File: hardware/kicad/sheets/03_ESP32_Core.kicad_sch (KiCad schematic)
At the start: 0 parts

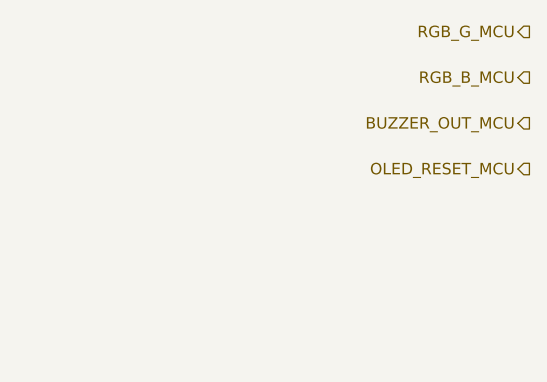
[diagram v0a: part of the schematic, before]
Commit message: Resolve Rev A power control interfaces
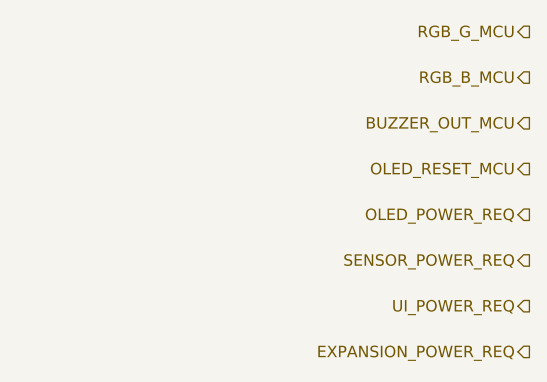
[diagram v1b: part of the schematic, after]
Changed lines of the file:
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@@
+    (effects (font (size 1.27 1.27)) (justify right))
+  )
+  (hierarchical_label "OLED_POWER_REQ" (shape output) (at 180 126.28 180)
+    (effects (font (size 1.27 1.27)) (justify right))
+  )
+  (hierarchical_label "SENSOR_POWER_REQ" (shape output) (at 180 131.36 180)
+    (effects (font (size 1.27 1.27)) (justify right))
+  )
+  (hierarchical_label "UI_POWER_REQ" (shape output) (at 180 136.44 180)
+    (effects (font (size 1.27 1.27)) (justify right))
+  )
+  (hierarchical_label "EXPANSION_POWER_REQ" (shape output) (at 180 141.52 180)
     (effects (font (size 1.27 1.27)) (justify right))
   )

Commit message: Implement ESP32-S3 core subsystem
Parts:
- added C1: 22 µF effective bulk, symbol IPC100:C
- added C2: 1 µF X7R, symbol IPC100:C
- added C3: 100 nF X7R, symbol IPC100:C
- added C4: 1 µF EN RC starting value, symbol IPC100:C
- added C5: 10 nF CT — 100 ms target, verify suffix/equation, symbol IPC100:C
- added C6: 100 nF supervisor bypass, symbol IPC100:C
- added R1: 10 kΩ EN/reset pull-up, symbol IPC100:R
- added R2: 10 kΩ GPIO0 boot pull-up, symbol IPC100:R
- added R3: 22 Ω USB D- tuning, symbol IPC100:R
- added R4: 22 Ω USB D+ tuning, symbol IPC100:R
- added R5: 499 Ω UART0 TX EMC series, symbol IPC100:R
- added SW1: RESET — momentary NO, symbol IPC100:SW
- added SW2: BOOT — momentary NO, symbol IPC100:SW
- added U1: ESP32-S3-WROOM-1-N8, symbol IPC100:ESP32S3WROOM1
- added U2: TPS389030-Q1 2.89 V typ / 100 ms target, symbol IPC100:TPS3890
- added U3: TPD2EUSB30 low-capacitance ESD boundary, symbol IPC100:TPD2EUSB30
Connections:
- net +3V3_CORE: now also C1.2, C2.2, C3.2, C6.2, R1.2, R2.2, U1.19 (GPIO11), U2.1 (VDD), U2.2 (SENSE), U2.3 (MR)
- net ARM_IN_COND: now also U1.9 (GPIO16)
- net AXIS1_LEN_MCU: now also U1.10 (GPIO17)
- net AXIS1_LPWM_MCU: now also U1.40 (GND)
- net AXIS1_REN_MCU: now also U1.11 (GPIO18)
- net AXIS1_RPWM_MCU: now also U1.41 (EPAD_GND)
- net AXIS2_LEN_MCU: now also U1.31 (GPIO38)
- net AXIS2_LPWM_MCU: now also U1.12 (GPIO8)
- net AXIS2_REN_MCU: now also U1.39 (GPIO1_ADC1_CH0)
- net AXIS2_RPWM_MCU: now also U1.13 (GPIO19_USB_D-)
- net BATTERY_SENSE: now also U1.23 (GPIO21)
- net ENCODER_A_COND: now also U1.3 (EN_CHIP_PU)
- net ENCODER_B_COND: now also U1.2 (3V3)
- net ENCODER_SW_COND: now also U1.1 (GND)
- net ESP_BOOT: now also R2.1, SW2.2, U1.35 (GPIO42_RESERVED)
- net ESP_EN: now also C4.2, R1.1, SW1.2, U1.18 (GPIO10), U2.6 (GND)
- net EXPANSION_POWER_REQ: now also U1.28 (GPIO35)
- net FIRE_IN_COND: now also U1.4 (GPIO4)
- net I2C_SCL: now also U1.37 (GPIO43_U0TXD)
- net I2C_SDA: now also U1.38 (GPIO2)
- net LIMIT_DOWN_COND: now also U1.14 (GPIO20_USB_D+)
- net LIMIT_LEFT_COND: now also U1.17 (GPIO9)
- net LIMIT_RIGHT_COND: now also U1.16 (GPIO46_STRAP)
- net LIMIT_UP_COND: now also U1.15 (GPIO3_STRAP)
- net OLED_POWER_REQ: now also U1.34 (GPIO41)
- net RELAY_CMD_MCU: now also U1.30 (GPIO37_RESERVED)
- net SENSOR_POWER_REQ: now also U1.33 (GPIO40)
- net STOP_IN_COND: now also U1.24 (GPIO47)
- net UART0_RX: now also U1.26 (GPIO45_STRAP)
- net UART0_TX: now also R5.1
- net UI_POWER_REQ: now also U1.29 (GPIO36)
- net USB_D+: now also R4.2, U3.1 (D-)
- net USB_D-: now also R3.2, U3.2 (D+)
- new net CORE_RESET_CT: C5.2, U2.5 (CT)
- new net GND: C1.1, C2.1, C3.1, C4.1, C5.1, C6.1, SW1.1, SW2.1, U1.20 (GPIO12), U1.21 (GPIO13), U1.22 (GPIO14), U2.4 (RESET_N), U3.3 (GND)
- new net UART0_TX_MCU: R5.2, U1.25 (GPIO48)
- new net USB_D+_MCU: R4.1, U1.7 (GPIO7)
- new net USB_D-_MCU: R3.1, U1.8 (GPIO15)
- no-connect marks 0 -> 5
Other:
- note added: "1 — ESP32-S3-WROOM-1-N8 CORE (8 MB QSPI FLASH, NO PSRAM, NO EXTERNAL CRYSTAL)"
- note added: "2 — CORE SUPPLY DECOUPLING (PLACE AT MODULE 3V3/GND PINS)"
- note added: "3 — CORE SUPERVISOR, EN/RESET, BOOT STRAP"
- note added: "4 — MCU-SIDE USB 2.0 SERIAL/JTAG AND UART0 RECOVERY"
- note added: "5 — HIERARCHICAL FUNCTIONAL INTERFACES (RAW GPIO IDENTIFIERS TERMINATE ABOVE)"
- note added: "Functional net names only cross the sheet boundary. MAIN_POWER_GOOD, MAIN_INPUT_VALID, POWER_FAULT_SUMMARY, RGB, buzzer, OLED reset, future communications, and physical connectors are intentionally absent."
- note added: "GPIO3 / GPIO45 / GPIO46 remain unconnected straps. GPIO37 / GPIO42 remain unconnected future reserve. EPAD and both module GND pins bond directly to the logic ground plane."
- note added: "Keep module antenna keepout free of copper, components, enclosure metal, and harnesses per Espressif guidance. Footprint and PCB keepout intentionally deferred."
- note added: "Native USB Serial/JTAG is the approved JTAG/debug path. No traditional JTAG pins or debugger connector are added. Sheet 09 owns USB-C, CC, shield, external pinout, and fixture contacts."
- note added: "No separate analog rail exists on ESP32-S3-WROOM-1-N8. The module integrates crystal, flash, and internal supply support; add no external oscillator or invented analog regulator."
- note added: "Normal boot: GPIO0 released high. Joint download recovery: hold BOOT/GPIO0 low, pulse RESET/EN low, release EN, then release BOOT. GPIO3/45/46 remain unloaded."
- note added: "RESET_VALID is the active-high, pulled-up supervisor release/EN node. It proves hardware reset release and readiness to begin instruction execution; it does not prove application initialization."
- note added: "UART0 RX is direct 3.3 V fixture input; the fixture shall never drive an unpowered module. UART0 TX may emit ROM boot messages. R5 follows Espressif's preliminary EMC guidance."
- note removed: "Detailed implementation intentionally deferred to subsequent engineering package."
- note removed: "PACKAGE 01 PLACEHOLDER — NO CIRCUITRY OR FOOTPRINTS"
- title: IPC-100 Rev A — 03 ESP32 Core -> IPC-100 Rev A — 03 ESP32-S3 Core, Boot, Programming & Recovery

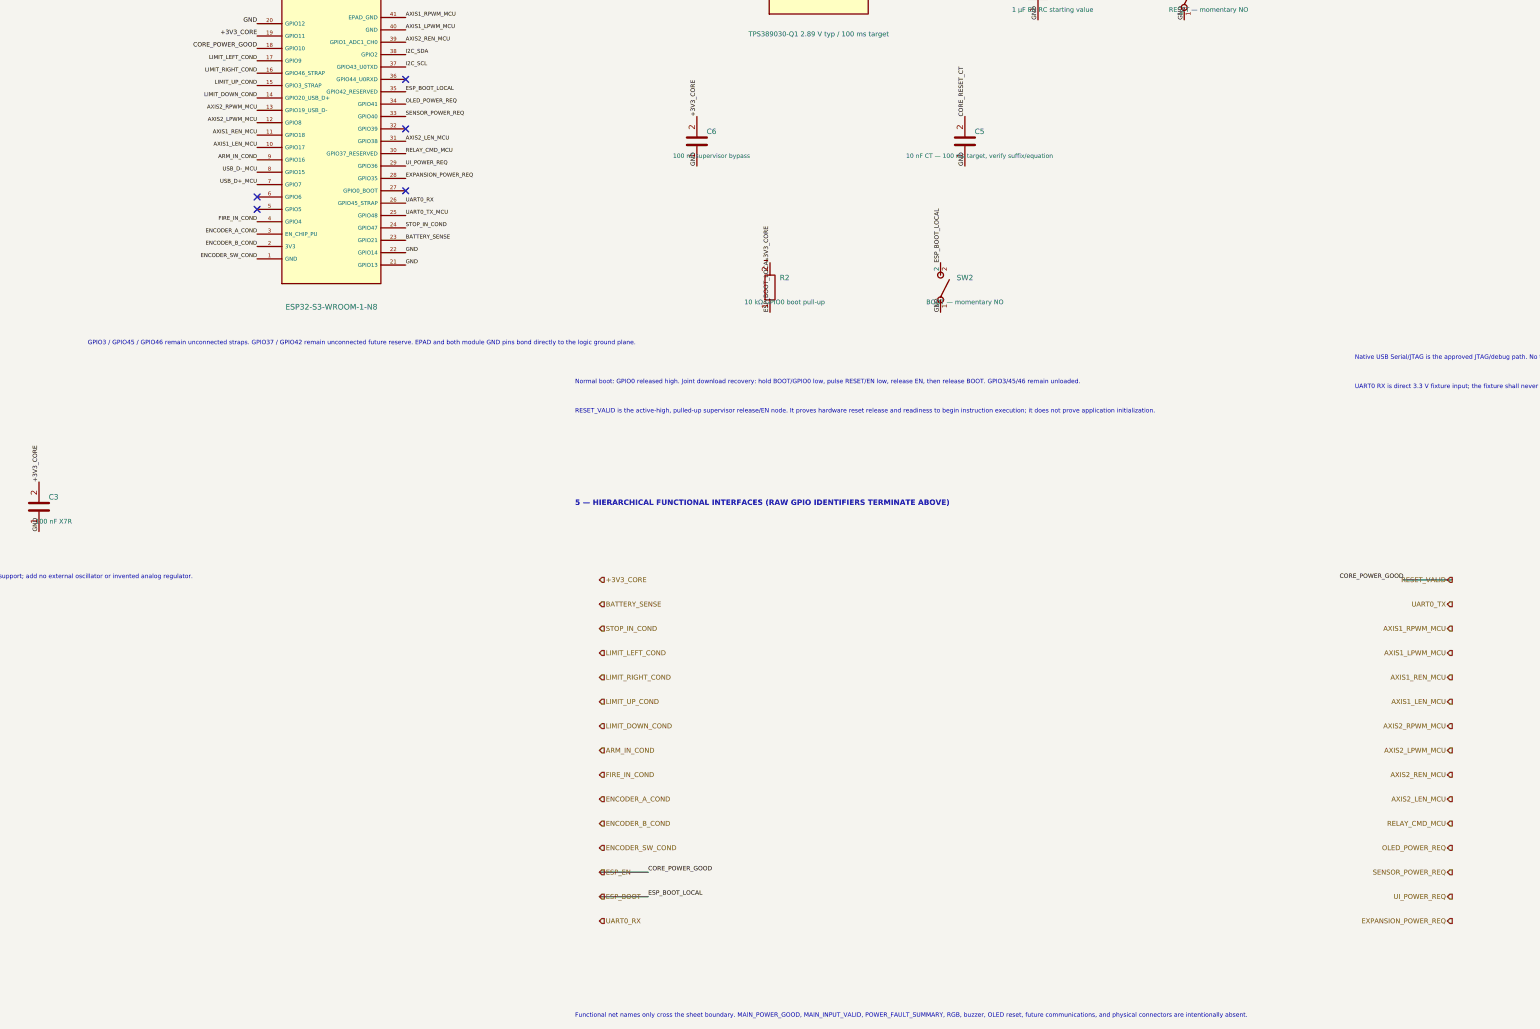
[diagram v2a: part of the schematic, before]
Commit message: Resolve independent watchdog service interface
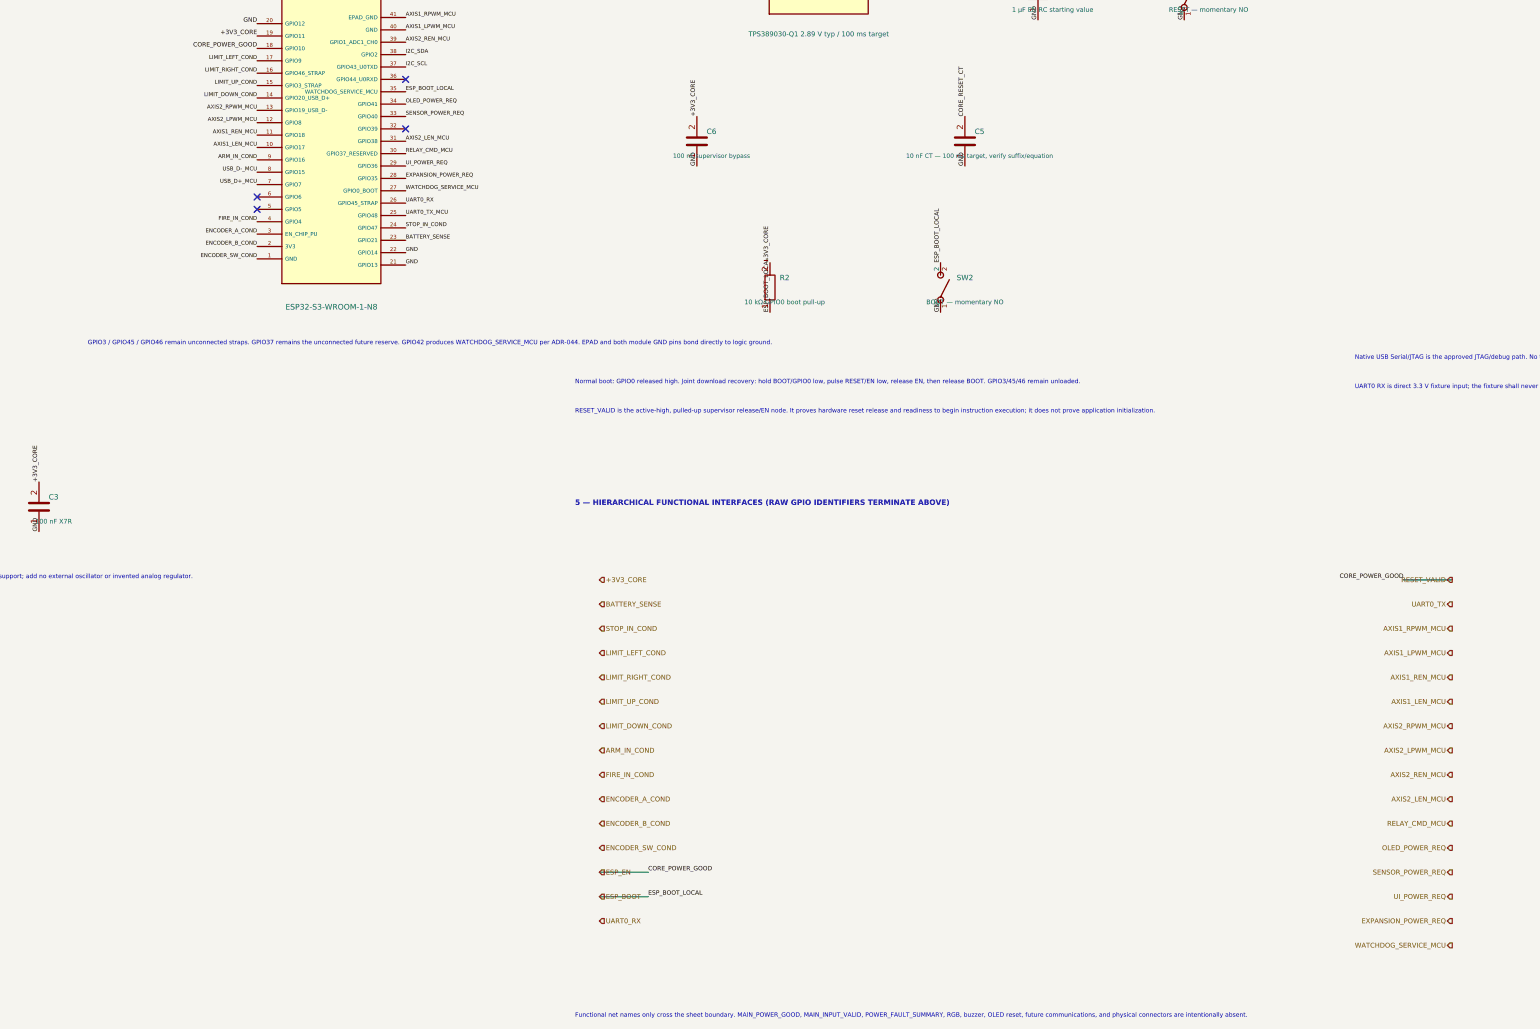
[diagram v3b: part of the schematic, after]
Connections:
- net WATCHDOG_SERVICE_MCU: now reaches U1.27 (GPIO0_BOOT)
- no-connect marks 5 -> 4
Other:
- note added: "GPIO3 / GPIO45 / GPIO46 remain unconnected straps. GPIO37 remains the unconnected future reserve. GPIO42 produces WATCHDOG_SERVICE_MCU per ADR-044. EPAD and both module GND pins bond directly to logic ground."
- note removed: "GPIO3 / GPIO45 / GPIO46 remain unconnected straps. GPIO37 / GPIO42 remain unconnected future reserve. EPAD and both module GND pins bond directly to the logic ground plane."
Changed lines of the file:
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@@
   (label "UI_POWER_REQ" (at 175.24 95.08 0) (effects (font (size 0.8 0.8)) (justify left bottom)))
   (label "EXPANSION_POWER_REQ" (at 175.24 97.62 0) (effects (font (size 0.8 0.8)) (justify left bottom)))
-  (no_connect (at 175.24 100.16))
+  (label "WATCHDOG_SERVICE_MCU" (at 175.24 100.16 0) (effects (font (size 0.8 0.8)) (justify left bottom)))
   (label "UART0_RX" (at 175.24 102.7 0) (effects (font (size 0.8 0.8)) (justify left bottom)))
   (label "UART0_TX_MCU" (at 175.24 105.24 0) (effects (font (size 0.8 0.8)) (justify left bottom)))
@@
   (label "GND" (at 175.24 112.86 0) (effects (font (size 0.8 0.8)) (justify left bottom)))
   (label "GND" (at 175.24 115.4 0) (effects (font (size 0.8 0.8)) (justify left bottom)))
-  (text "GPIO3 / GPIO45 / GPIO46 remain unconnected straps. GPIO37 / GPIO42 remain unconnected future reserve. EPAD and both module GND pins bond directly to the logic ground plane." (at 110 132 0) (effects (font (size 0.9 0.9)) (justify left bottom)))
+  (text "GPIO3 / GPIO45 / GPIO46 remain unconnected straps. GPIO37 remains the unconnected future reserve. GPIO42 produces WATCHDOG_SERVICE_MCU per ADR-044. EPAD and both module GND pins bond directly to logic ground." (at 110 132 0) (effects (font (size 0.9 0.9)) (justify left bottom)))
   (text "2 — CORE SUPPLY DECOUPLING (PLACE AT MODULE 3V3/GND PINS)" (at 20 145 0) (effects (font (size 1.1 1.1) (bold yes)) (justify left bottom)))
   (symbol (lib_id "IPC100:C") (at 35 165 0) (unit 1) (exclude_from_sim no) (in_bom yes) (on_board yes) (dnp no)
@@
   (hierarchical_label "AXIS2_LEN_MCU" (shape output) (at 390 225 180) (effects (font (size 1 1)) (justify right)))
   (hierarchical_label "RELAY_CMD_MCU" (shape output) (at 390 230 180) (effects (font (size 1 1)) (justify right)))
+  (hierarchical_label "WATCHDOG_SERVICE_MCU" (shape output) (at 390 255 180) (effects (font (size 1 1)) (justify right)))
   (hierarchical_label "OLED_POWER_REQ" (shape output) (at 390 235 180) (effects (font (size 1 1)) (justify right)))
   (hierarchical_label "SENSOR_POWER_REQ" (shape output) (at 390 240 180) (effects (font (size 1 1)) (justify right)))

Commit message: Normalize Rev A reference designators
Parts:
- renumbered C1 to C301, C2 to C302, C3 to C303, C4 to C304, C5 to C305, C6 to C306, R1 to R301, R2 to R302, R3 to R303, R4 to R304, R5 to R305, SW1 to SW301, SW2 to SW302, U1 to U301, U2 to U302, U3 to U303

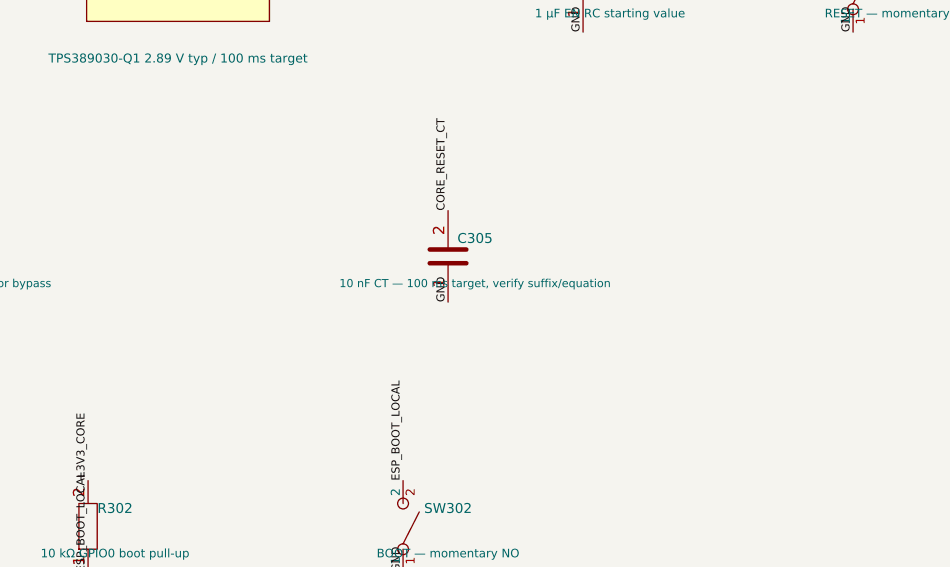
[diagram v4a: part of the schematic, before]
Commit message: Correct C305 supervisor timing
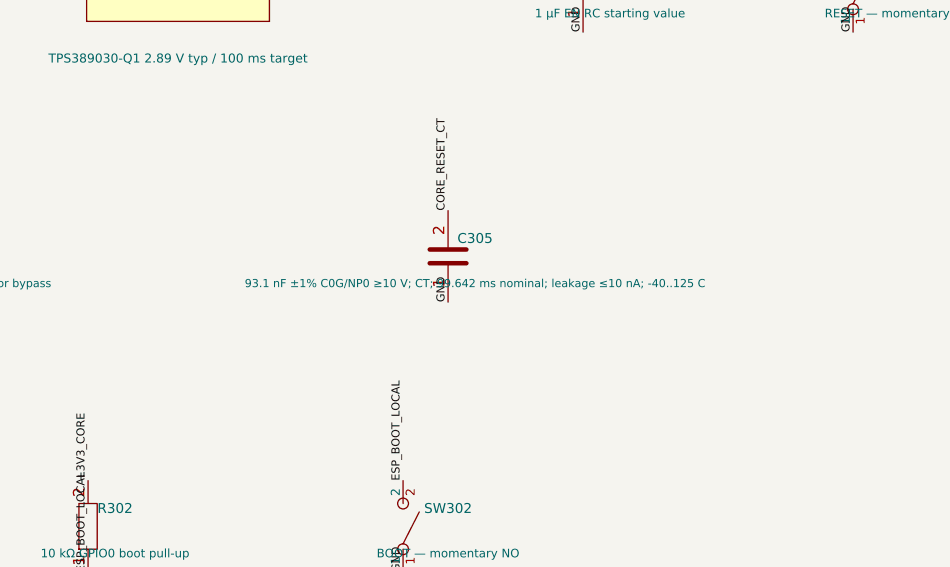
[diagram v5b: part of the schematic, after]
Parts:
- C305: value 10 nF CT — 100 ms target, verify suffix/equation -> 93.1 nF ±1% C0G/NP0 ≥10 V; CT; 99.642 ms nominal; leakage ≤10 nA; -40..125 C
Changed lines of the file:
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@@
   (label "GND" (at 335 65.08 90) (effects (font (size 0.9 0.9)) (justify left bottom)))
   (symbol (lib_id "IPC100:C") (at 290 90 0) (unit 1) (exclude_from_sim no) (in_bom yes) (on_board yes) (dnp no)
- (property "Reference" "C305" (at 293 88 0) (effects (font (size 1.1 1.1)))) (property "Value" "10 nF CT — 100 ms target, verify suffix/equation" (at 293 93 0) (effects (font (size 0.9 0.9)))) (property "Footprint" "" (at 290 90 0) (effects (font (size 1 1)) hide)) (property "Datasheet" "" (at 290 90 0) (effects (font (size 1 1)) hide))
+ (property "Reference" "C305" (at 293 88 0) (effects (font (size 1.1 1.1)))) (property "Value" "93.1 nF ±1% C0G/NP0 ≥10 V; CT; 99.642 ms nominal; leakage ≤10 nA; -40..125 C" (at 293 93 0) (effects (font (size 0.9 0.9)))) (property "Footprint" "" (at 290 90 0) (effects (font (size 1 1)) hide)) (property "Datasheet" "https://www.ti.com/lit/ds/symlink/tps3890-q1.pdf" (at 290 90 0) (effects (font (size 1 1)) hide))
     (pin "1") (pin "2") (instances (project "IPC-100" (path "/10000000-0000-4000-8000-000000000001/10000000-0000-4000-8000-000000000025" (reference "C305") (unit 1))))
   )
